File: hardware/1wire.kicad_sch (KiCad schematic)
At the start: 0 parts

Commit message: block refactoring
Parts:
- added C10: 1nF, Capacitor_SMD:C_0603_1608Metric, symbol Device:C
- added C7: 1uF, Capacitor_SMD:C_0603_1608Metric, symbol Device:C
- added D16: RCLAMP0502B, Package_TO_SOT_SMD:SOT-416, symbol Power_Protection:RCLAMP0502B
- added J1: Conn_01x03/1Wire, Connector_JST:JST_PH_B4B-PH-K_1x03_P2.00mm_Vertical, symbol Connector_Generic:Conn_01x03
- added JP5: SolderJumper_3_Bridged12, Jumper:SolderJumper-3_P1.3mm_Bridged12_Pad1.0x1.5mm_NumberLabels, symbol Jumper:SolderJumper_3_Bridged12
- added R1: 4.7k, Resistor_SMD:R_0603_1608Metric, symbol Device:R
- added R15: 150, Resistor_SMD:R_0603_1608Metric, symbol Device:R
- added TP1: TestPoint, TestPoint:TestPoint_Pad_1.0x1.0mm, symbol Connector:TestPoint
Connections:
- new net: JP5.3 (B), R15.2
- new net 1WIRE_3V3: C7.1, D16.2 (K2), J1.2 (Pin_2), R1.2
- new net 1WIRE_DQ: C10.1, JP5.1 (A), R15.1, TP1.1
- new net DQ: D16.1 (K1), J1.3 (Pin_3), JP5.2 (C), R1.1
- new net GND: C10.2, C7.2, D16.3 (A), J1.1 (Pin_1)
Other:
- note added: "1-wire"
- note added: "Filter for long network lengths"

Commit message: moving subsheets to blocks
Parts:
- removed TP1: TestPoint, TestPoint:TestPoint_Pad_1.0x1.0mm, symbol Connector:TestPoint
- J1: footprint Connector_JST:JST_PH_B4B-PH-K_1x03_P2.00mm_Vertical -> Connector_JST:JST_PH_B3B-PH-K_1x03_P2.00mm_Vertical
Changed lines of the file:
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@@
   (junction (at 100.33 60.96) (diameter 0) (color 0 0 0 0)
   )
-  (junction (at 179.07 60.96) (diameter 0) (color 0 0 0 0)
-  )
   (junction (at 88.9 60.96) (diameter 0) (color 0 0 0 0)
   )
@@
     (stroke (width 0) (type default))
   )
-  (wire (pts (xy 172.72 60.96) (xy 179.07 60.96))
+  (wire (pts (xy 172.72 60.96) (xy 181.61 60.96))
     (stroke (width 0) (type default))
   )
@@
     (stroke (width 0) (type default))
   )
-  (wire (pts (xy 179.07 60.96) (xy 181.61 60.96))
-    (stroke (width 0) (type default))
-  )
   (wire (pts (xy 172.72 60.96) (xy 172.72 69.85))
     (stroke (width 0) (type default))
@@
   )
   (wire (pts (xy 73.66 60.96) (xy 88.9 60.96))
-    (stroke (width 0) (type default))
-  )
-  (wire (pts (xy 179.07 45.72) (xy 179.07 60.96))
     (stroke (width 0) (type default))
   )
@@
         (path "/3d8a08e7-1222-4d27-bd08-b4e997cf9472/a93e91c4-1cc1-4b97-a9d5-eeb8eb0c6542"
           (reference "R15") (unit 1)
-        )
-      )
-    )
-  )
-  (symbol (lib_id "Connector:TestPoint") (at 179.07 45.72 0) (unit 1)
-    (in_bom yes) (on_board yes) (dnp no) (fields_autoplaced)
-    (property "Reference" "TP1" (at 181.61 41.148 0)
-      (effects (font (size 1.27 1.27)) (justify left))
-    )
-    (property "Value" "TestPoint" (at 181.61 43.688 0)
-      (effects (font (size 1.27 1.27)) (justify left))
-    )
-    (property "Footprint" "TestPoint:TestPoint_Pad_1.0x1.0mm" (at 184.15 45.72 0)
-      (effects (font (size 1.27 1.27)) hide)
-    )
-    (property "Datasheet" "~" (at 184.15 45.72 0)
-      (effects (font (size 1.27 1.27)) hide)
-    )
-    (pin "1")
-    (instances
-      (project "esp32-multitool"
-        (path "/3d8a08e7-1222-4d27-bd08-b4e997cf9472/a93e91c4-1cc1-4b97-a9d5-eeb8eb0c6542"
-          (reference "TP1") (unit 1)
         )
       )
@@
       (effects (font (size 1.27 1.27)) (justify left))
     )
-    (property "Footprint" "Connector_JST:JST_PH_B4B-PH-K_1x03_P2.00mm_Vertical" (at 58.42 73.66 0)
-      (effects (font (size 1.27 1.27)) hide)
-    )
+    (property "Footprint" "Connector_JST:JST_PH_B3B-PH-K_1x03_P2.00mm_Vertical" (at 58.42 73.66 0)
+      (effects (font (size 1.27 1.27)) hide)
+    )

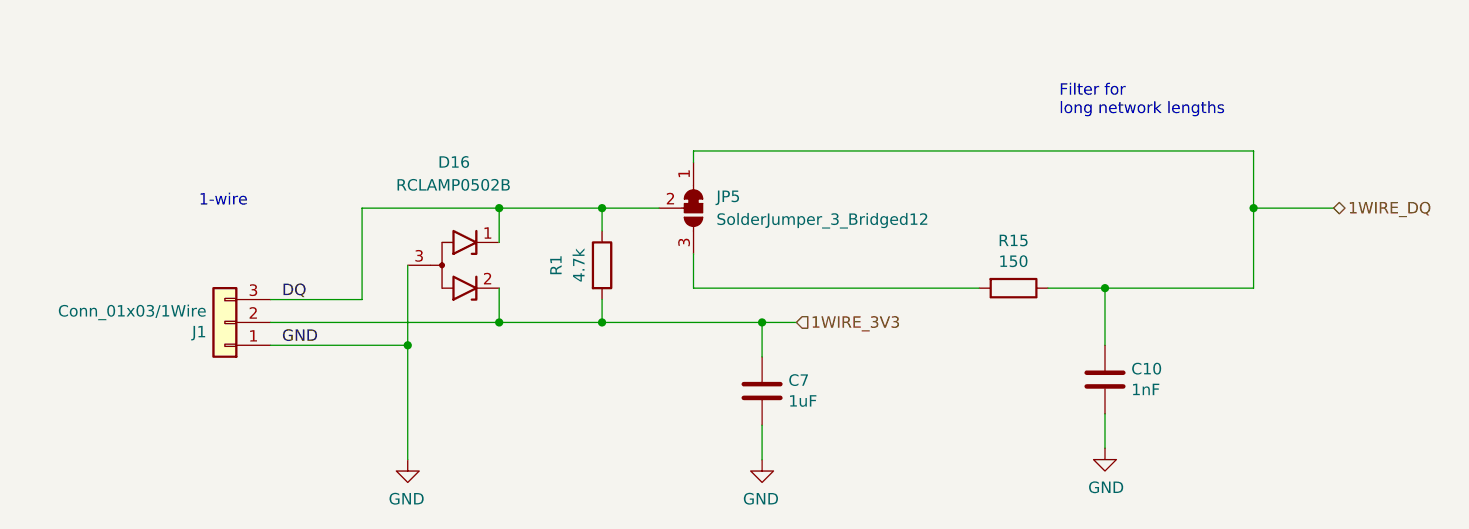
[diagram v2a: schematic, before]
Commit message: Added 3D models and ran freerouting
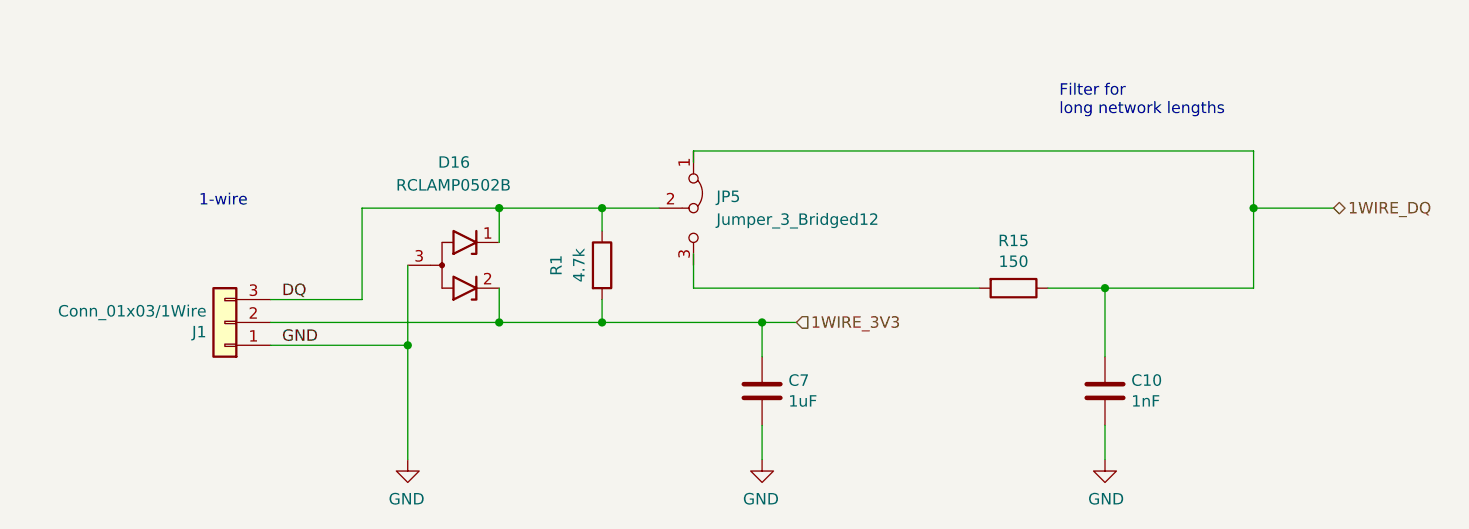
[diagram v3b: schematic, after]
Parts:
- C10, C7: footprint Capacitor_SMD:C_0603_1608Metric -> Capacitor_SMD:C_0805_2012Metric
- JP5: value SolderJumper_3_Bridged12 -> Jumper_3_Bridged12; footprint Jumper:SolderJumper-3_P1.3mm_Bridged12_Pad1.0x1.5mm_NumberLabels -> Connector_PinHeader_2.54mm:PinHeader_1x03_P2.54mm_Vertical; symbol Jumper:SolderJumper_3_Bridged12 -> Jumper:Jumper_3_Bridged12
- R1, R15: footprint Resistor_SMD:R_0603_1608Metric -> Resistor_SMD:R_0805_2012Metric
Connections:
- net at R15.2: no longer JP5.3 (B)
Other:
- moved on the sheet: C10
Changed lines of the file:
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@@
     (stroke (width 0) (type default))
   )
-  (wire (pts (xy 156.21 69.85) (xy 156.21 76.2))
-    (stroke (width 0) (type default))
-  )
-  (wire (pts (xy 156.21 83.82) (xy 156.21 87.63))
+  (wire (pts (xy 156.21 69.85) (xy 156.21 77.47))
+    (stroke (width 0) (type default))
+  )
+  (wire (pts (xy 156.21 85.09) (xy 156.21 88.9))
     (stroke (width 0) (type default))
   )
@@
     (effects (font (size 1.27 1.27)) (justify left))
   )
-  (symbol (lib_id "power:GND") (at 156.21 87.63 0) (unit 1)
-    (in_bom yes) (on_board yes) (dnp no)
-    (property "Reference" "#PWR040" (at 156.21 93.98 0)
-      (effects (font (size 1.27 1.27)) hide)
-    )
-    (property "Value" "GND" (at 156.337 92.0242 0)
-      (effects (font (size 1.27 1.27)))
-    )
-    (property "Footprint" "" (at 156.21 87.63 0)
-      (effects (font (size 1.27 1.27)) hide)
-    )
-    (property "Datasheet" "" (at 156.21 87.63 0)
+  (symbol (lib_id "power:GND") (at 156.21 88.9 0) (unit 1)
+    (in_bom yes) (on_board yes) (dnp no)
+    (property "Reference" "#PWR040" (at 156.21 95.25 0)
+      (effects (font (size 1.27 1.27)) hide)
+    )
+    (property "Value" "GND" (at 156.337 93.2942 0)
+      (effects (font (size 1.27 1.27)))
+    )
+    (property "Footprint" "" (at 156.21 88.9 0)
+      (effects (font (size 1.27 1.27)) hide)
+    )
+    (property "Datasheet" "" (at 156.21 88.9 0)
       (effects (font (size 1.27 1.27)) hide)
     )
@@
     )
   )
-  (symbol (lib_id "Device:C") (at 156.21 80.01 0) (unit 1)
-    (in_bom yes) (on_board yes) (dnp no)
-    (property "Reference" "C10" (at 159.131 78.8416 0)
-      (effects (font (size 1.27 1.27)) (justify left))
-    )
-    (property "Value" "1nF" (at 159.131 81.153 0)
-      (effects (font (size 1.27 1.27)) (justify left))
-    )
-    (property "Footprint" "Capacitor_SMD:C_0603_1608Metric" (at 157.1752 83.82 0)
-      (effects (font (size 1.27 1.27)) hide)
-    )
-    (property "Datasheet" "~" (at 156.21 80.01 0)
-      (effects (font (size 1.27 1.27)) hide)
-    )
-    (property "LCSC" "C1588" (at 156.21 80.01 0)
-      (effects (font (size 1.27 1.27)) hide)
-    )
-    (property "Part" "CL10B102KB8NNNC" (at 156.21 80.01 0)
-      (effects (font (size 1.27 1.27)) hide)
-    )
-    (property "Cost" "0.0028" (at 156.21 80.01 0)
+  (symbol (lib_id "Device:C") (at 156.21 81.28 0) (unit 1)
+    (in_bom yes) (on_board yes) (dnp no)
+    (property "Reference" "C10" (at 159.131 80.1116 0)
+      (effects (font (size 1.27 1.27)) (justify left))
+    )
+    (property "Value" "1nF" (at 159.131 82.423 0)
+      (effects (font (size 1.27 1.27)) (justify left))
+    )
+    (property "Footprint" "Capacitor_SMD:C_0805_2012Metric" (at 157.1752 85.09 0)
+      (effects (font (size 1.27 1.27)) hide)
+    )
+    (property "Datasheet" "~" (at 156.21 81.28 0)
+      (effects (font (size 1.27 1.27)) hide)
+    )
+    (property "LCSC" "C1588" (at 156.21 81.28 0)
+      (effects (font (size 1.27 1.27)) hide)
+    )
+    (property "Part" "CL10B102KB8NNNC" (at 156.21 81.28 0)
+      (effects (font (size 1.27 1.27)) hide)
+    )
+    (property "Cost" "0.0028" (at 156.21 81.28 0)
       (effects (font (size 1.27 1.27)) hide)
     )
@@
       (effects (font (size 1.27 1.27)))
     )
-    (property "Footprint" "Resistor_SMD:R_0603_1608Metric" (at 146.05 68.072 90)
+    (property "Footprint" "Resistor_SMD:R_0805_2012Metric" (at 146.05 68.072 90)
       (effects (font (size 1.27 1.27)) hide)
     )
@@
       (effects (font (size 1.27 1.27)))
     )
-    (property "Footprint" "Resistor_SMD:R_0603_1608Metric" (at 98.552 67.31 90)
+    (property "Footprint" "Resistor_SMD:R_0805_2012Metric" (at 98.552 67.31 90)
       (effects (font (size 1.27 1.27)) hide)
     )
@@
     )
   )
-  (symbol (lib_id "Jumper:SolderJumper_3_Bridged12") (at 110.49 60.96 270) (unit 1)
+  (symbol (lib_id "Jumper:Jumper_3_Bridged12") (at 110.49 60.96 270) (unit 1)
     (in_bom yes) (on_board yes) (dnp no) (fields_autoplaced)
     (property "Reference" "JP5" (at 113.03 59.69 90)
       (effects (font (size 1.27 1.27)) (justify left))
     )
-    (property "Value" "SolderJumper_3_Bridged12" (at 113.03 62.23 90)
-      (effects (font (size 1.27 1.27)) (justify left))
-    )
-    (property "Footprint" "Jumper:SolderJumper-3_P1.3mm_Bridged12_Pad1.0x1.5mm_NumberLabels" (at 110.49 60.96 0)
+    (property "Value" "Jumper_3_Bridged12" (at 113.03 62.23 90)
+      (effects (font (size 1.27 1.27)) (justify left))
+    )
+    (property "Footprint" "Connector_PinHeader_2.54mm:PinHeader_1x03_P2.54mm_Vertical" (at 110.49 60.96 0)
       (effects (font (size 1.27 1.27)) hide)
     )
@@
       (effects (font (size 1.27 1.27)) (justify left))
     )
-    (property "Footprint" "Capacitor_SMD:C_0603_1608Metric" (at 119.0752 85.09 0)
-      (effects (font (size 1.27 1.27)) hide)
-    )
+    (property "Footprint" "Capacitor_SMD:C_0805_2012Metric" (at 119.0752 85.09 0)
+      (effects (font (size 1.27 1.27)) hide)
+    )
